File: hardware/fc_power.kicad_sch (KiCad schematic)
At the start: 35 parts, among them U3 LMR51430YFDDCR, U4 LMR51430YFDDCR, U6 LP5912-1.8DRVR, U7 LP5912-3.3DRVR

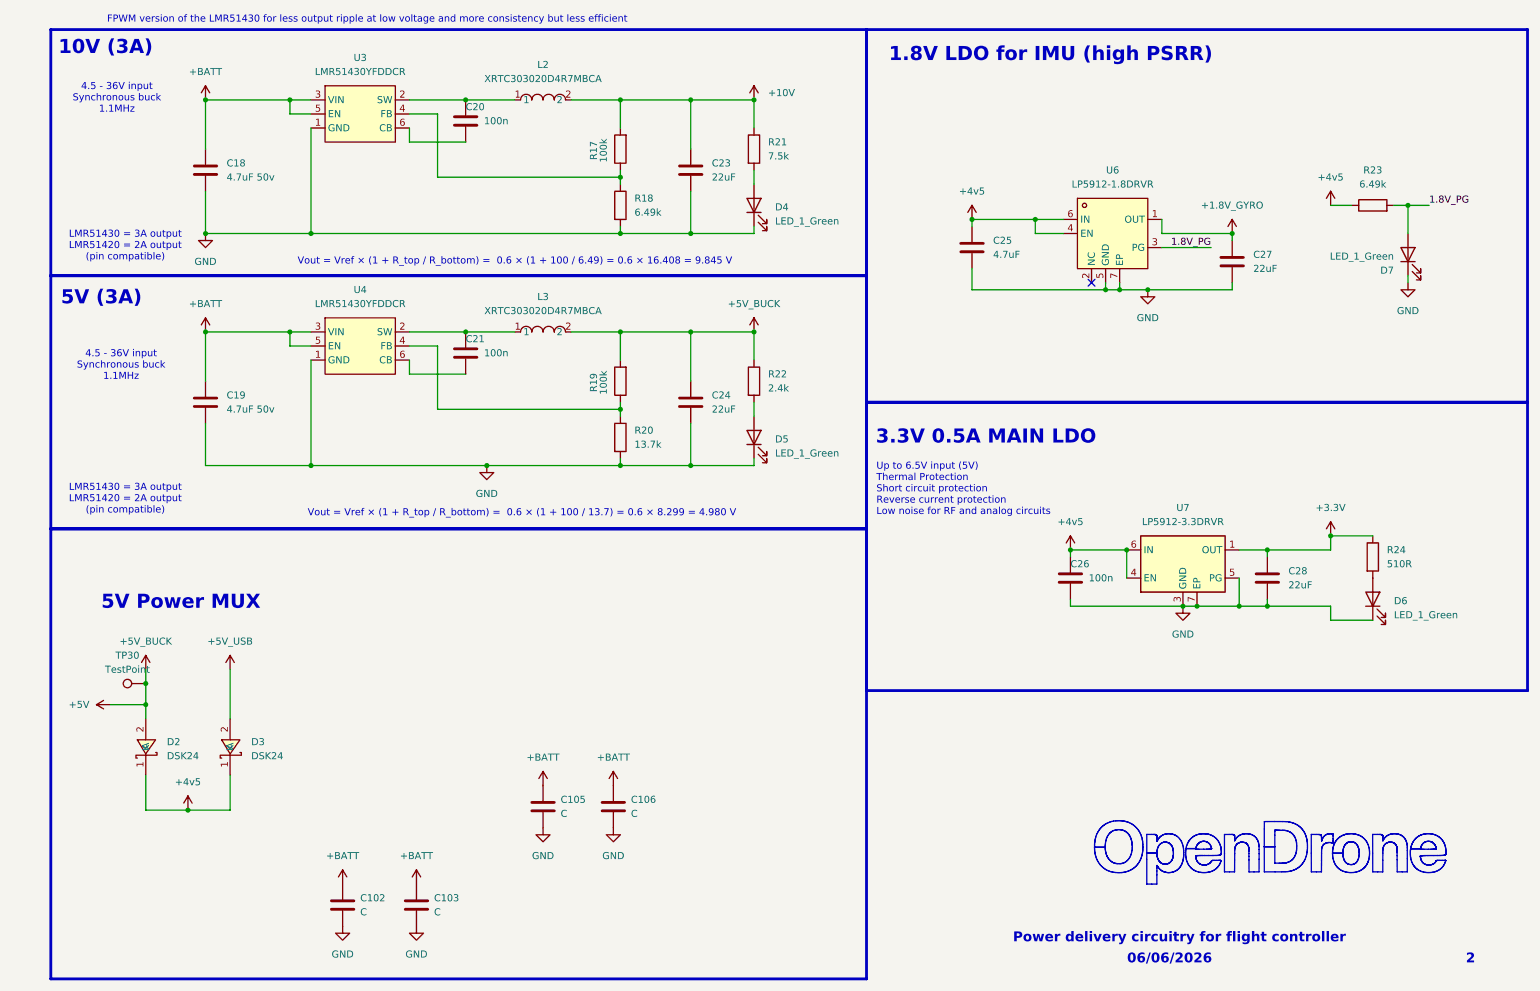
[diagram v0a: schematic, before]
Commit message: Circuit: B3 bulk caps and ESP32-C3FH4, LDO caps, BMI270 aux pins, BOOTSEL 1k, unused pads
CIRCUIT_REVIEW B3, S2, S4, S5 and decision D9; LAYOUT_REVIEW 5.3 (pure
clean-up). Values and parts from hardware/KiCad-Library/PARTS-USED.md.

- B3: the 16 +BATT bulk caps had value "C" and no part. C90-C103 (0805)
  4.7uF 50V X5R CL21A475KBQNNNE (C98192, already C18/C19); C105/C106 (1206)
  4.7uF 50V X7R TCC1206X7R475K500HT (C380366, OpenESC).
- D9/B3: U22 is ESP32-C3FH4 (C2858491, in-package flash), as its NC SPI pins
  require; its in-package-flash pads 19, 21-24 deleted per instance (20 was
  already gone). L4 MPN MLZ2012M150WT000 (TDK, SX1281 reference BOM, LCSC not
  in the catalogue); D9 MPN/manufacturer/LCSC from the catalogue.
- S2, LP5912 windows (CIN > 0.5 uF effective, COUT 0.7-10 uF): U7 COUT C28
  22uF -> 1uF CL05A105KA5NQNC; U6 COUT C27 22uF -> 4.7uF CL05A475MP5NRNC;
  U7 CIN C26 100nF -> 1uF GRM033R61A105ME44D in the existing 0201 (an 0402
  does not fit beside U7 without moving parts; ~0.5 uF effective at 4.6 V,
  so it is marginal until U7 moves to the Core in R2, decision S1).
- S4: BMI270 U8 ASDx/ASCx (pins 2/3) were on GND, which the datasheet
  forbids; now +3.3V (VDDIO), valid for the LSM6DSV16X option too.
  Schematic: the GND drop replaced by a +3.3V symbol. Core: pads 2/3 and the
  via between them re-netted, 0.15 mm In3 stub to the In3 +3.3V pour.
- S5: BOOTSEL resistor R7 10k -> 1k (0201WMF1001TEE, C270365): 10k with the
  32k minimum pull-up gave 0.79 V against VIL 0.8 V.
- LAYOUT_REVIEW 5.3, pads on no net with nothing attached: U13/U15/U17/U19
  (AT32F421) 3, 8, 9, 12, 23, 24, 26-28; U14/U16/U18/U20 (NSG2065Q) NC 5, 7,
  8, 21; U7 NC 2; U21 6 (XTB, TCXO), 9, 10 (DIO2/3); Core U2 55-59 (QSPI,
  in-package flash). 60 pads in all; U8 kept for joint symmetry. AT32
  firmware must keep the dropped pins as outputs or pulled.
- Footprint values and fields synced from the schematic for the changed refs.

Deferred: RX LED D9 to +4v5 (S10). +4v5 copper is 1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
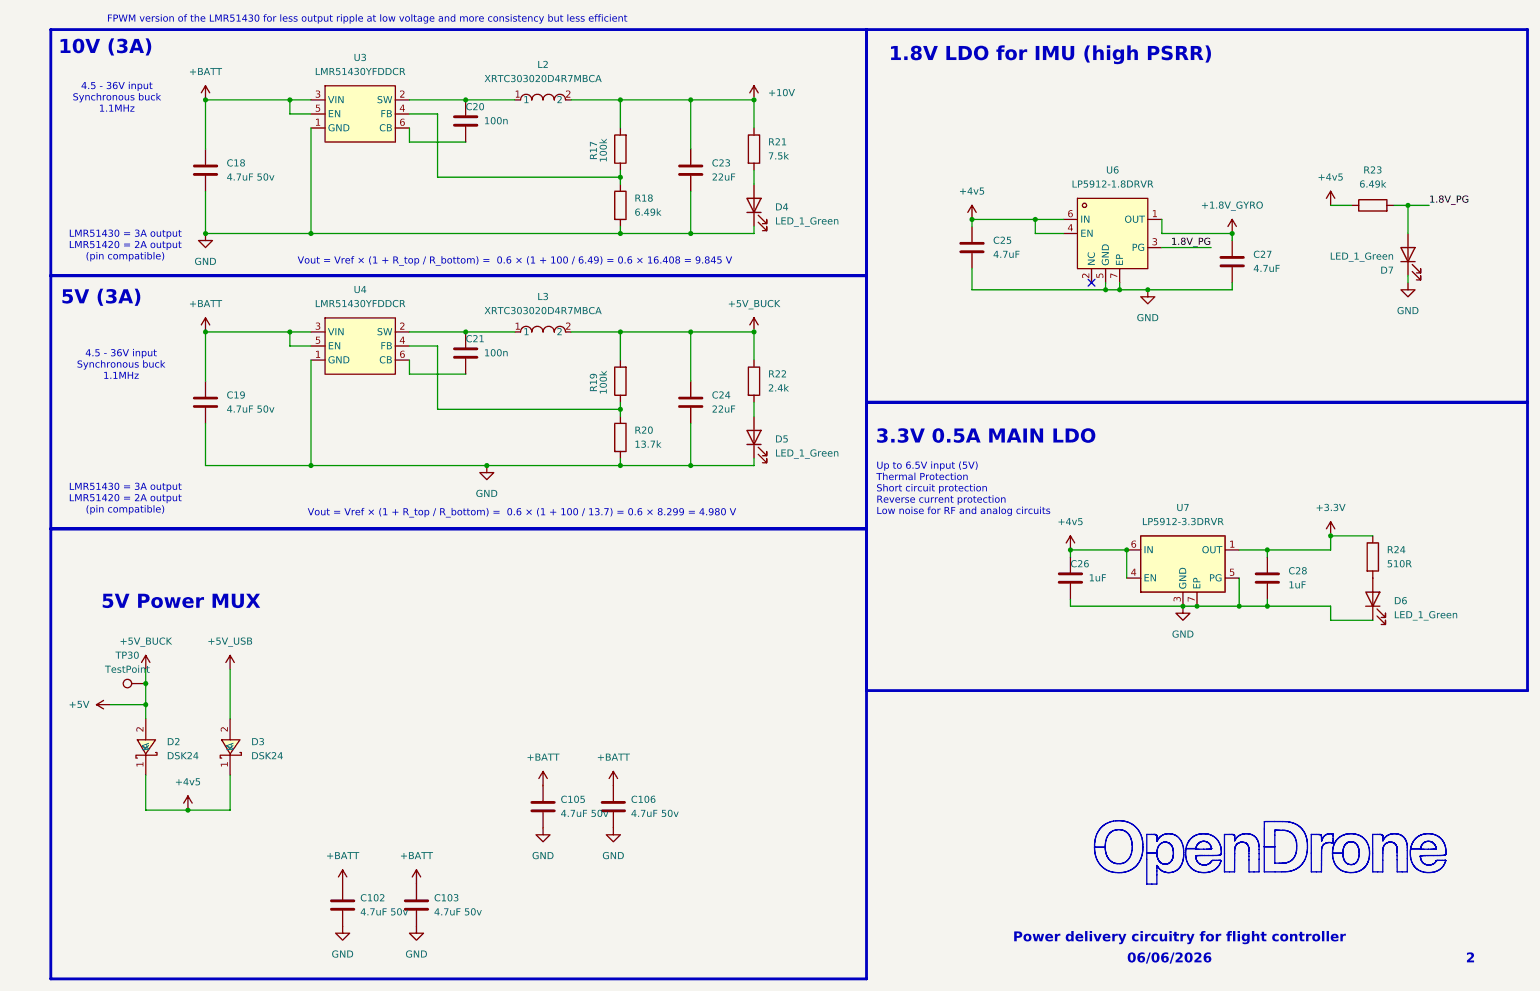
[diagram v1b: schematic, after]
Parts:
- C102, C103: value C -> 4.7uF 50v; LCSC (none) -> C98192; MPN (none) -> CL21A475KBQNNNE; Manufacturer (none) -> Samsung Electro-Mechanics
- C105, C106: value C -> 4.7uF 50v; LCSC (none) -> C380366; MPN (none) -> TCC1206X7R475K500HT; Manufacturer (none) -> CCTC
- C26: value 100n -> 1uF; LCSC C76939 -> C76935; MPN GRM033R61E104KE14D -> GRM033R61A105ME44D
- C27: value 22uF -> 4.7uF; LCSC C415703 -> C23733; MPN GRM155R60J226ME11D -> CL05A475MP5NRNC; Manufacturer Murata -> Samsung Electro-Mechanics
- C28: value 22uF -> 1uF; LCSC C415703 -> C52923; MPN GRM155R60J226ME11D -> CL05A105KA5NQNC; Manufacturer Murata -> Samsung Electro-Mechanics
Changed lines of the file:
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@@
 			)
 		)
-		(property "Value" "C"
+		(property "Value" "4.7uF 50v"
 			(at 106.045 167.0049 0)
 			(show_name no)
@@
 			)
 		)
+		(property "LCSC" "C380366"
+			(at 106.045 167.0049 0)
+			(hide yes)
+			(show_name no)
+			(do_not_autoplace no)
+			(effects
+				(font
+					(size 1.27 1.27)
+				)
+				(justify left)
+			)
+		)
+		(property "MPN" "TCC1206X7R475K500HT"
+			(at 106.045 167.0049 0)
+			(hide yes)
+			(show_name no)
+			(do_not_autoplace no)
+			(effects
+				(font
+					(size 1.27 1.27)
+				)
+				(justify left)
+			)
+		)
+		(property "Manufacturer" "CCTC"
+			(at 106.045 167.0049 0)
+			(hide yes)
+			(show_name no)
+			(do_not_autoplace no)
+			(effects
+				(font
+					(size 1.27 1.27)
+				)
+				(justify left)
+			)
+		)
 		(pin "2"
 		)
@@
 			)
 		)
-		(property "Value" "C"
+		(property "Value" "4.7uF 50v"
 			(at 69.85 184.7849 0)
 			(show_name no)
@@
 			)
 		)
+		(property "LCSC" "C98192"
+			(at 69.85 184.7849 0)
+			(hide yes)
+			(show_name no)
+			(do_not_autoplace no)
+			(effects
+				(font
+					(size 1.27 1.27)
+				)
+				(justify left)
+			)
+		)
+		(property "MPN" "CL21A475KBQNNNE"
+			(at 69.85 184.7849 0)
+			(hide yes)
+			(show_name no)
+			(do_not_autoplace no)
+			(effects
+				(font
+					(size 1.27 1.27)
+				)
+				(justify left)
+			)
+		)
+		(property "Manufacturer" "Samsung Electro-Mechanics"
+			(at 69.85 184.7849 0)
+			(hide yes)
+			(show_name no)
+			(do_not_autoplace no)
+			(effects
+				(font
+					(size 1.27 1.27)
+				)
+				(justify left)
+			)
+		)
 		(pin "2"
 		)
@@
 			)
 		)
-		(property "Value" "100n"
+		(property "Value" "1uF"
 			(at 201.422 124.46 0)
 			(show_name no)
@@
 			)
 		)
-		(property "LCSC" "C76939"
+		(property "LCSC" "C76935"
 			(at 198.12 124.46 0)
 			(hide yes)
@@
 			)
 		)
-		(property "MPN" "GRM033R61E104KE14D"
+		(property "MPN" "GRM033R61A105ME44D"
 			(at 0 15.24 0)
 			(hide yes)
@@
 			)
 		)
-		(property "Value" "C"
+		(property "Value" "4.7uF 50v"
 			(at 118.745 167.0049 0)
 			(show_name no)
@@
 			)
 		)
+		(property "LCSC" "C380366"
+			(at 118.745 167.0049 0)
+			(hide yes)
+			(show_name no)
+			(do_not_autoplace no)
+			(effects
+				(font
+					(size 1.27 1.27)
+				)
+				(justify left)
+			)
+		)
+		(property "MPN" "TCC1206X7R475K500HT"
+			(at 118.745 167.0049 0)
+			(hide yes)
+			(show_name no)
+			(do_not_autoplace no)
+			(effects
+				(font
+					(size 1.27 1.27)
+				)
+				(justify left)
+			)
+		)
+		(property "Manufacturer" "CCTC"
+			(at 118.745 167.0049 0)
+			(hide yes)
+			(show_name no)
+			(do_not_autoplace no)
+			(effects
+				(font
+					(size 1.27 1.27)
+				)
+				(justify left)
+			)
+		)
 		(pin "2"
 		)
@@
 			)
 		)
-		(property "Value" "C"
+		(property "Value" "4.7uF 50v"
 			(at 83.185 184.7849 0)
 			(show_name no)
@@
 			)
 		)
+		(property "LCSC" "C98192"
+			(at 83.185 184.7849 0)
+			(hide yes)
+			(show_name no)
+			(do_not_autoplace no)
+			(effects
+				(font
+					(size 1.27 1.27)
+				)
+				(justify left)
+			)
+		)
+		(property "MPN" "CL21A475KBQNNNE"
+			(at 83.185 184.7849 0)
+			(hide yes)
+			(show_name no)
+			(do_not_autoplace no)
+			(effects
+				(font
+					(size 1.27 1.27)
+				)
+				(justify left)
+			)
+		)
+		(property "Manufacturer" "Samsung Electro-Mechanics"
+			(at 83.185 184.7849 0)
+			(hide yes)
+			(show_name no)
+			(do_not_autoplace no)
+			(effects
+				(font
+					(size 1.27 1.27)
+				)
+				(justify left)
+			)
+		)
 		(pin "2"
 		)
@@
 			)
 		)
-		(property "Value" "22uF"
+		(property "Value" "4.7uF"
 			(at 231.14 68.5799 0)
 			(show_name no)
@@
 			)
 		)
-		(property "LCSC" "C415703"
+		(property "LCSC" "C23733"
 			(at 227.33 67.31 0)
 			(hide yes)
@@
 			)
 		)
-		(property "MPN" "GRM155R60J226ME11D"
+		(property "MPN" "CL05A475MP5NRNC"
 			(at 7.62 2.54 0)
 			(hide yes)
@@
 			)
 		)
-		(property "Manufacturer" "Murata"
+		(property "Manufacturer" "Samsung Electro-Mechanics"
 			(at 7.62 2.54 0)
 			(hide yes)
@@
 			)
 		)
-		(property "Value" "22uF"
+		(property "Value" "1uF"
 			(at 237.49 125.7299 0)
 			(show_name no)
@@
 			)
 		)
-		(property "LCSC" "C415703"
+		(property "LCSC" "C52923"
 			(at 233.68 124.46 0)
 			(hide yes)
@@
 			)
 		)
-		(property "MPN" "GRM155R60J226ME11D"
+		(property "MPN" "CL05A105KA5NQNC"
 			(at 0 15.24 0)
 			(hide yes)
@@
 			)
 		)
-		(property "Manufacturer" "Murata"
+		(property "Manufacturer" "Samsung Electro-Mechanics"
 			(at 0 15.24 0)
 			(hide yes)

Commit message: Owner rules: no component silk, pad labels and values, no wordmark text, MPN + maker on every BOM line
The owner rules adopted in PLAN.md (pcb-agent-commons, 2026-10-06), applied
where they are local edits:

- No component silkscreen. J91's reference was the only visible one (Core
  B.Silkscreen, under the LGA) and is hidden. Footprint silk graphics removed
  per instance: Base 234, Core 72. Kept: connector outlines and pin-1 marks
  (USB1, U12 SH-6, Card1, JP1) and the LGA pin-1 marks (J90, J91). Base
  lib_footprint_mismatch warnings 31 -> 40 as a result.
- Solder-pad labels: Core J53 (GND) had none, now "gnd" in the style of J52's
  label. The SH-6 per-pin labels ("10v gnd T0", "R0 gnd R1") become the port
  name "DJI" (connectors: name and pin-1 mark only). Core J48-J51 have no room:
  0.5 mm to J44 above, 0.93 mm to the board edge below. CIRCUIT_REVIEW 8.3
  moves them off the LGA in R2, so their labels go with that move.
- Pad values: all 40 solder-pad symbols said "5V". Each now carries its
  function (5V, GND, LED, BUZ+/BUZ-, 10V, 4V5, CAM, VTX, SCL, SDA, TX0/RX0,
  TX1/RX1, PIO_TX0/PIO_RX0; off-board J19 ADC2, J22 GND, J46/J47 NC).
- No "Drone" text: the "OpenDrone" wordmark on Core F.Silkscreen (9 filled
  polygons in two groups) is removed; a TODO for the incutec wordmark from the
  brand repo sits on User.Comments (not fabricated). No other such text on any
  copper, mask or silk layer of either board.
- BOM: lines missing manufacturer or MPN 41 -> 1. MPNs come from
  PARTS-USED.md by LCSC number. Manufacturers come from the catalogue symbol,
  this design's spelling for the same MPN family, or the committed datasheet
  (NSIC, Sofng, Jiangsu Changjing, Hirose). Still open: Rsense2
  ASR-S-3-0.2F (C695806), whose manufacturer nothing in the catalogue states.
  U24 (board outline) and TP9 (BOOT solder pad) are not parts: excluded from
  BOM and position files.
- 0201 default / minimal capacitance: respected in the circuit commit (C26
  stays 0201; no belt-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
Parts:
- R18, R23: MPN (none) -> AF0201FR-076K49L; Manufacturer (none) -> YAGEO
- R21: MPN (none) -> RC0201FR-077K5L; Manufacturer (none) -> YAGEO
- R22: MPN (none) -> RTT012401FTH; Manufacturer (none) -> RALEC
- R24: MPN (none) -> RC0201FR-07510RL; Manufacturer (none) -> YAGEO
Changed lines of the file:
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@@
 			)
 		)
-		(property "MPN" ""
+		(property "MPN" "AF0201FR-076K49L"
 			(at 195.58 173.99 0)
 			(hide yes)
@@
 			)
 		)
-		(property "Manufacturer" ""
+		(property "Manufacturer" "YAGEO"
 			(at 195.58 173.99 0)
 			(hide yes)
@@
 			)
 		)
-		(property "MPN" ""
+		(property "MPN" "RTT012401FTH"
 			(at -116.84 49.53 0)
 			(hide yes)
@@
 			)
 		)
-		(property "Manufacturer" ""
+		(property "Manufacturer" "RALEC"
 			(at -116.84 49.53 0)
 			(hide yes)
@@
 			)
 		)
-		(property "MPN" ""
+		(property "MPN" "AF0201FR-076K49L"
 			(at 0 0 0)
 			(hide yes)
@@
 			)
 		)
-		(property "Manufacturer" ""
+		(property "Manufacturer" "YAGEO"
 			(at 0 0 0)
 			(hide yes)
@@
 			)
 		)
-		(property "MPN" ""
+		(property "MPN" "RC0201FR-077K5L"
 			(at 0 0 0)
 			(hide yes)
@@
 			)
 		)
-		(property "Manufacturer" ""
+		(property "Manufacturer" "YAGEO"
 			(at 0 0 0)
 			(hide yes)
@@
 			)
 		)
-		(property "MPN" ""
+		(property "MPN" "RC0201FR-07510RL"
 			(at 0 16.51 0)
 			(hide yes)
@@
 			)
 		)
-		(property "Manufacturer" ""
+		(property "Manufacturer" "YAGEO"
 			(at 0 16.51 0)
 			(hide yes)
